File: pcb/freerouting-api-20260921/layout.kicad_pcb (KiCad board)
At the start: 4 copper layers, 36 x 76 mm, 115 parts, among them J1 B2B-PH-K-S, J3 B2B-PH-K-S, J4 104031-0811, Q1 AO3400A, Q2 AO3400A, SW1 PTS841GKSMTR LFS, SW2 JS202011AQN, U1 113991114, U10 SN74CBTLV3245APWR, U11 SN74CBTLV3245APWR, U3 MAX17048G+T10, U4 BMI270, U5 TPS61023DRLR, U6 AP2112K-3.3TRG1, U7 TPS22918DBVR, U8 TPS22918DBVR, U9 TPS22918DBVR

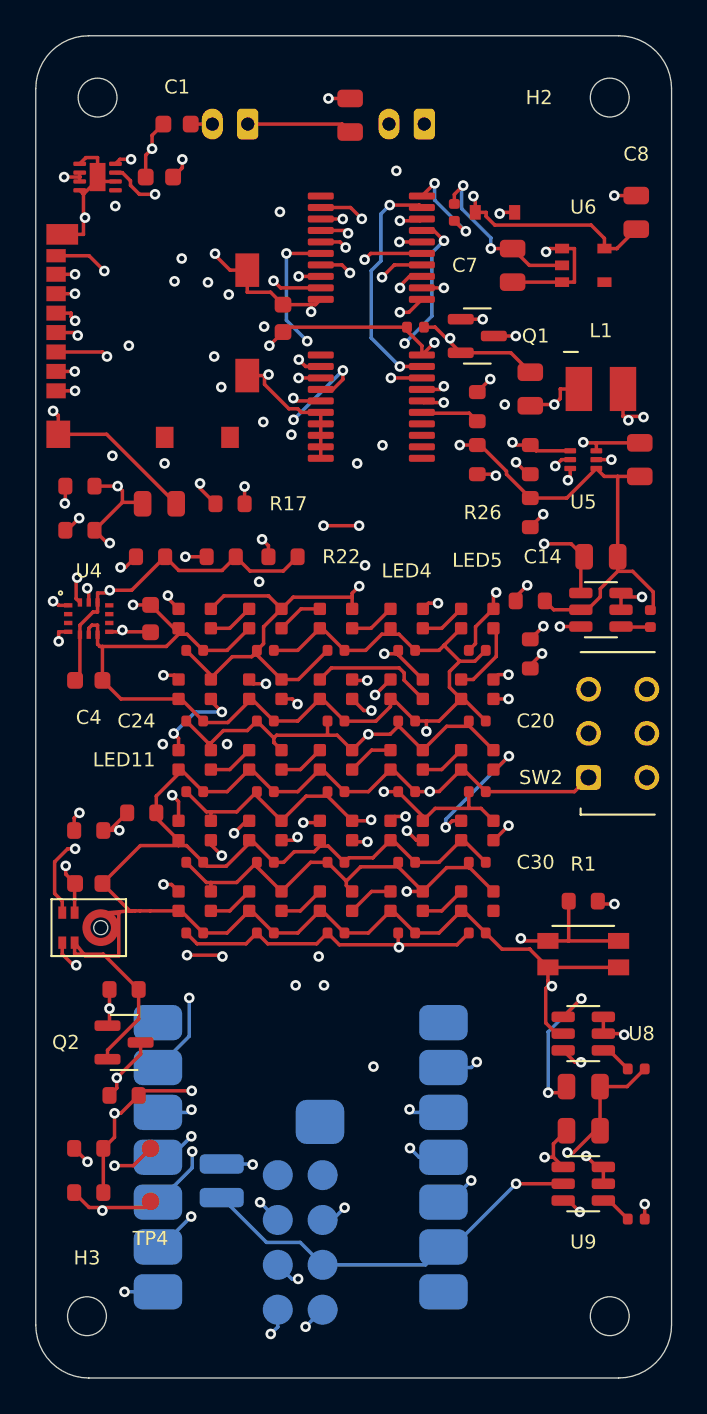
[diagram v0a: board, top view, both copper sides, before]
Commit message: Update board configuration, BOM, and documentation for new XIAO ESP32S3
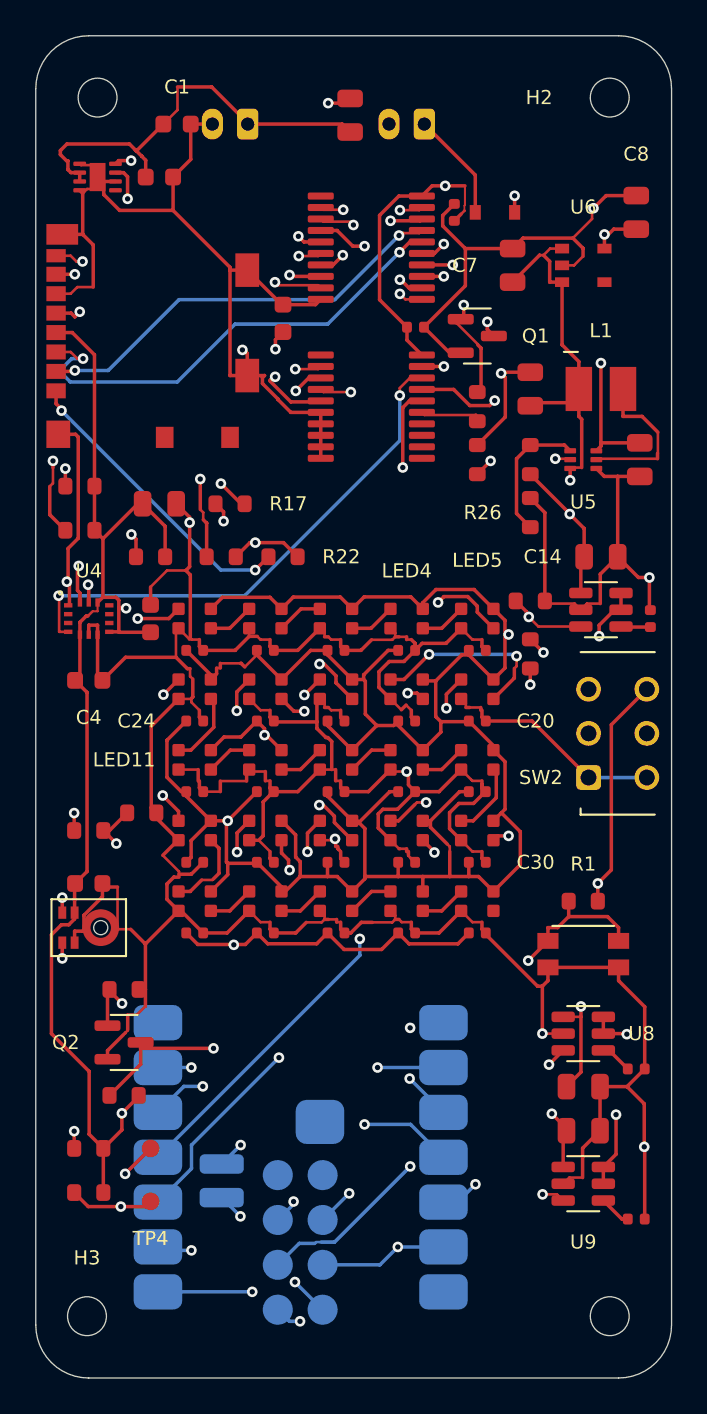
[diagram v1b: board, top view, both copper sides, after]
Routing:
- net GND: track 412.7 -> 483.7 mm, vias 21 -> 13
- net V3V3: track 148.5 -> 161.1 mm, vias 14 -> 6
- net SD_MISO: track 41.6 -> 52.0 mm, vias 4 -> 3
- net RECORD_BUTTON: track 41.0 -> 51.1 mm, vias 3 -> 2
- net LED_CHAIN_5: track 4.19 -> 12.4 mm, vias 0 -> 2
- net V3V3_AON: track 37.7 -> 45.7 mm, vias 4 -> 3
- net SD_CS: track 38.0 -> 30.8 mm, vias 4 -> 3
- net LED_DATA: track 24.0 -> 30.5 mm
- net HOST_PDM_CLK: track 63.5 -> 57.0 mm, vias 7 -> 2
- net BOOST_5V: track 19.0 -> 24.6 mm, vias 3 -> 2
- net MOTOR_GATE: track 12.5 -> 17.7 mm, vias 3 -> 2
- net VBAT_PERIPH: track 67.3 -> 62.3 mm, vias 4 -> 2
- net SD_CLK: track 22.7 -> 17.7 mm, vias 3 -> 2
- net HOST_SD_MISO: track 54.8 -> 59.5 mm
- net MOTOR_3V3: track 17.1 -> 21.8 mm
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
